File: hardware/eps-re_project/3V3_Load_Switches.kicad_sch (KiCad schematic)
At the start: 28 parts, among them U1 LMV321RIYLT, U10 SI2329DS-T1-GE3, U2 INA199C1DCKR, U3 INA199C1DCKR, U4 INA199C1DCKR, U5 NVTFS5116PLWFTAG, U6 NVTFS5116PLWFTAG, U7 NVTFS5116PLWFTAG, U8 SI2329DS-T1-GE3, U9 SI2329DS-T1-GE3

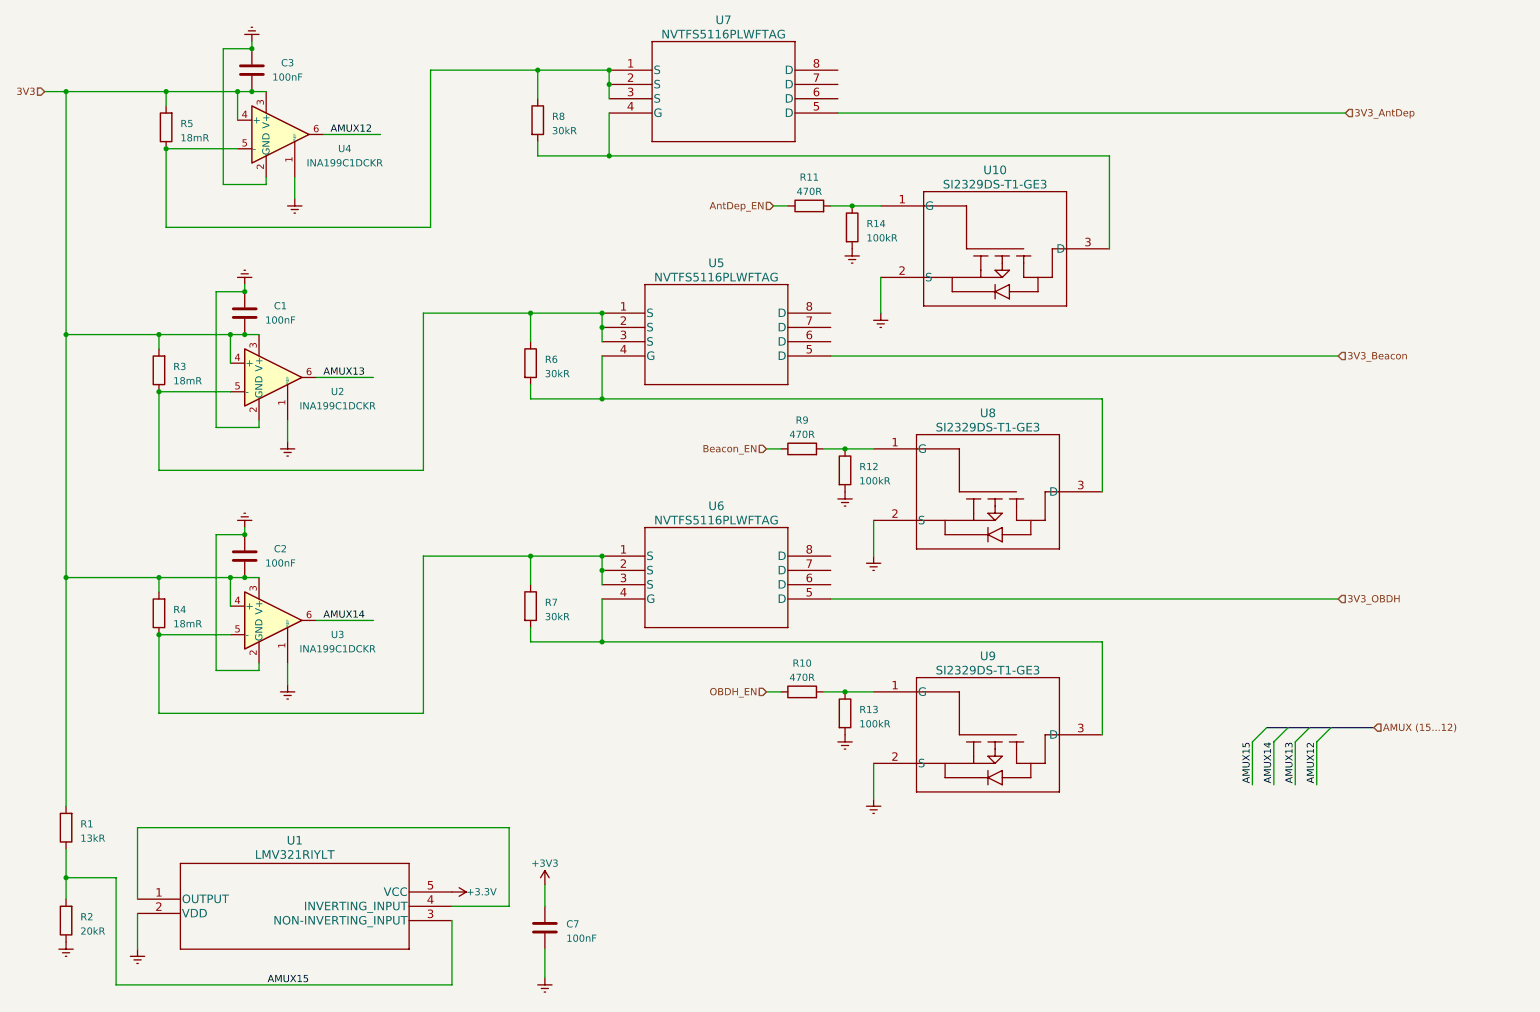
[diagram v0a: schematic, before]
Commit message: hardware: Restructuring the circuit, modifying symbols, footprints and other corrections
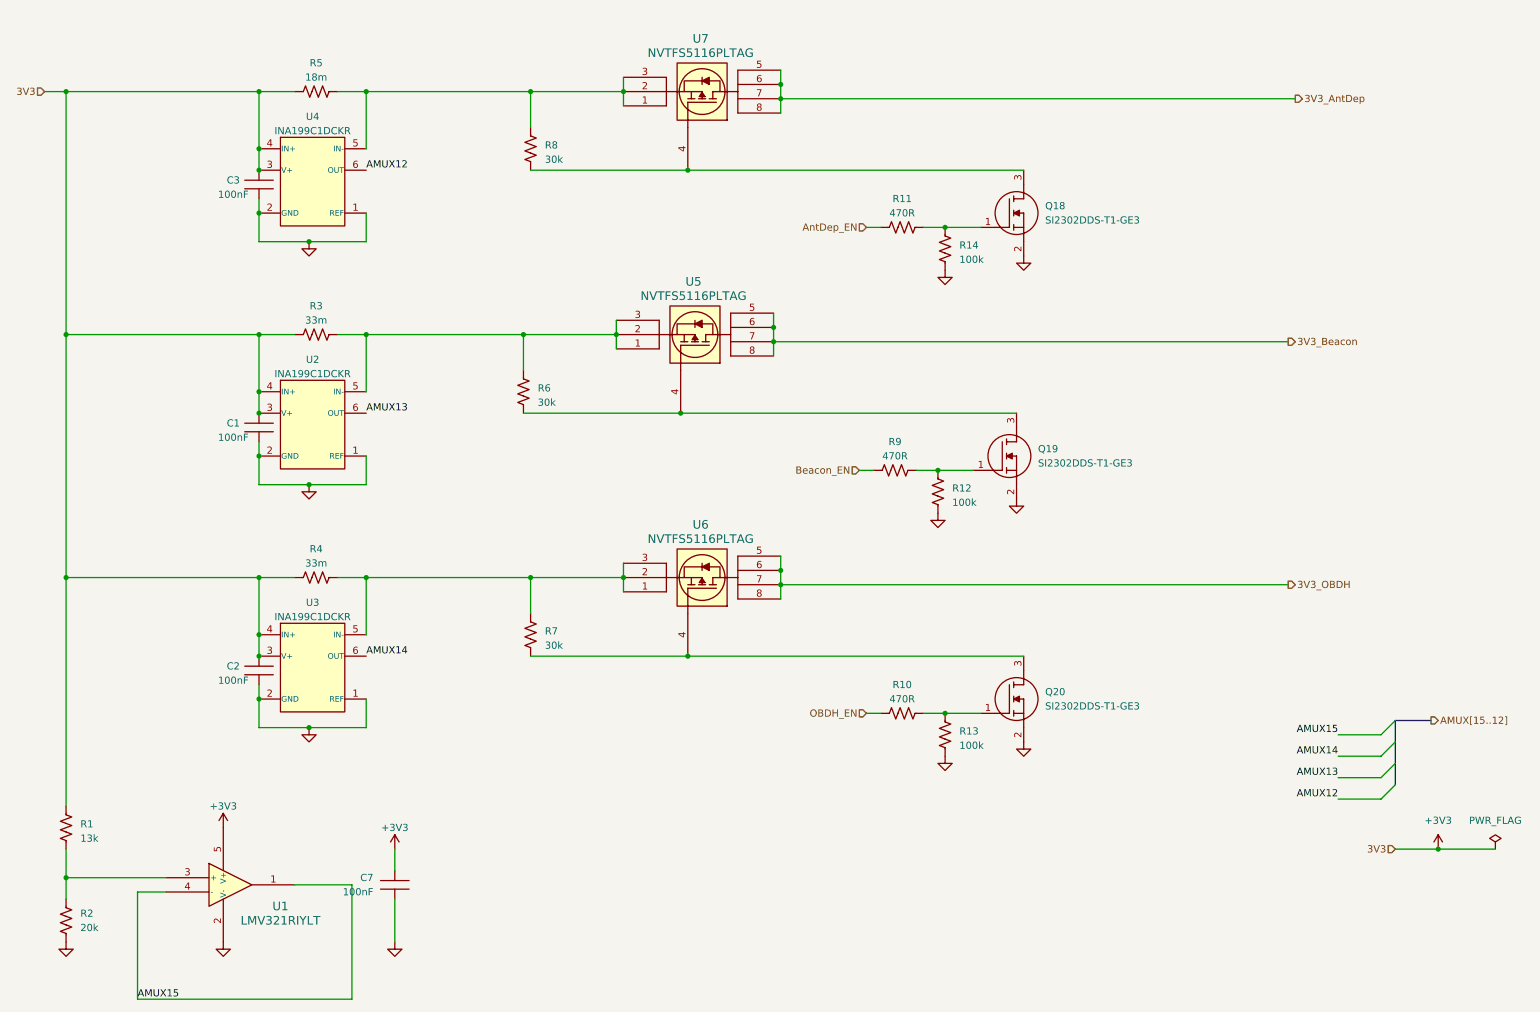
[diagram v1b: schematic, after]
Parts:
- removed C1, C2, C3: 100nF, symbol Device:C
- removed R10, R9: 470R, symbol Device:R
- removed R12, R13: 100kR, symbol Device:R
- removed R3, R4: 18mR, symbol Device:R
- removed R6, R7: 30kR, symbol Device:R
- removed U10, U8, U9: SI2329DS-T1-GE3, SOT_DS-T1-GE3_VIS, symbol SI2329DS-T1-GE3:SI2329DS-T1-GE3
- removed U2, U3, U4: INA199C1DCKR, Package_TO_SOT_SMD:SOT-363_SC-70-6, symbol Amplifier_Current:INA199xxDCK
- removed U5, U6, U7: NVTFS5116PLWFTAG, WDFN8_3P30X3P30_ONS, symbol NVTFS5116PLWFTAG:NVTFS5116PLWFTAG
- added C1, C2, C3: 100nF, footprints:C0603C104K5RACTU, symbol C0603C104K5RACTU:C0603C104K5RACTU
- added Q18, Q19, Q20: SI2302DDS-T1-GE3, footprints:SI2302DDS-T1-GE3, symbol SI2302DDS-T1-GE3:SI2302DDS-T1-GE3
- added R10, R9: 470R, symbol Device:R_US
- added R12, R13: 100k, symbol Device:R_US
- added R3, R4: 33m, symbol Device:R_US
- added R6, R7: 30k, symbol Device:R_US
- added U2, U3, U4: INA199C1DCKR, footprints:INA199C1DCKR, symbol INA199C1DCKR:INA199xxDCK
- added U5, U6, U7: NVTFS5116PLTAG, footprints:NVTFS5116PLTAG, symbol NVTFS5116PLWFTAG:NVTFS5116PLTAG
- C7: footprint (none) -> footprints:C0603C104K5RACTU; symbol Device:C -> C0603C104K5RACTU:C0603C104K5RACTU; automotive (none) -> Yes; automotive grade (none) -> Grade 1; capacitance (none) -> 0.10 μF; category (none) -> Cap; device class L1 (none) -> Passive Components; device class L2 (none) -> Capacitors; device class L3 (none) -> Ceramic Capacitors; digikey description (none) -> CAP CER 0.1UF 50V X7R 0603; digikey part number (none) -> 399-5089-2-ND; height (none) -> 0.87mm; lead free (none) -> Yes; library id (none) -> 73022d3323b2b2b8; manufacturer (none) -> KEMET; material (none) -> Ceramic; mouser part number (none) -> 80-C0603C104K5R7867; package (none) -> 0603; rohs (none) -> Yes; temperature characteristic (none) -> X7R; temperature coefficient (none) -> 30ppm/°C; temperature range high (none) -> +125°C; temperature range low (none) -> -55°C; tolerance (none) -> 0.1; voltage rating (none) -> 50 V
- R1: value 13kR -> 13k; symbol Device:R -> Device:R_US
- R11: symbol Device:R -> Device:R_US
- R14: value 100kR -> 100k; symbol Device:R -> Device:R_US
- R2: value 20kR -> 20k; symbol Device:R -> Device:R_US
- R5: value 18mR -> 18m; symbol Device:R -> Device:R_US
- R8: value 30kR -> 30k; symbol Device:R -> Device:R_US
- U1: footprint SOT23-5_STM -> footprints:LMV321RIYLT
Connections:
- net +3.3V is gone; now on net +3V3: U1.5 (V+)
- net 3V3 is gone; now on net +3V3: R1.2, R5.2
- net +3V3: now also C1.1, C2.1, C3.1, R3.2, R4.2, U2.3 (V+), U2.4 (IN+), U3.3 (V+), U3.4 (IN+), U4.3 (V+), U4.4 (IN+)
- net 3V3_AntDep: now also U7.5, U7.6, U7.7, U7.8
- net 3V3_Beacon: now also U5.5, U5.6, U5.7, U5.8
- net 3V3_OBDH: now also U6.5, U6.6, U6.7, U6.8
- net AMUX12: now also U4.6 (OUT)
- net AMUX13: now also U2.6 (OUT)
- net AMUX14: now also U3.6 (OUT)
- net AMUX15: now also U1.1, U1.4 (-); no longer R1.1, R2.2, U1.3 (NON-INVERTING_INPUT)
- net Beacon_EN: now also R9.1
- net OBDH_EN: now also R10.1
- net at R5.1, R8.1: now also U4.5 (IN-), U7.1, U7.2, U7.3
- net at R8.2: now also Q18.3 (D), U7.4
- net at R11.2, R14.1: now also Q18.1 (G)
- net Earth renamed GND
- net GND: now also C1.2, C2.2, C3.2, Q18.2 (S), Q19.2 (S), Q20.2 (S), R12.2, R13.2, U2.1 (REF), U2.2 (GND), U3.1 (REF), U3.2 (GND), U4.1 (REF), U4.2 (GND)
- new net: R4.1, R7.1, U3.5 (IN-), U6.1, U6.2, U6.3
- new net: Q20.3 (D), R7.2, U6.4
- new net: R3.1, R6.1, U2.5 (IN-), U5.1, U5.2, U5.3
- new net: R1.1, R2.2, U1.3 (+)
- new net: Q20.1 (G), R10.2, R13.1
- new net: Q19.3 (D), R6.2, U5.4
- new net: Q19.1 (G), R12.1, R9.2
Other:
- moved on the sheet: C7
